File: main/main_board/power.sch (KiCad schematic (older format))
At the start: 18 parts

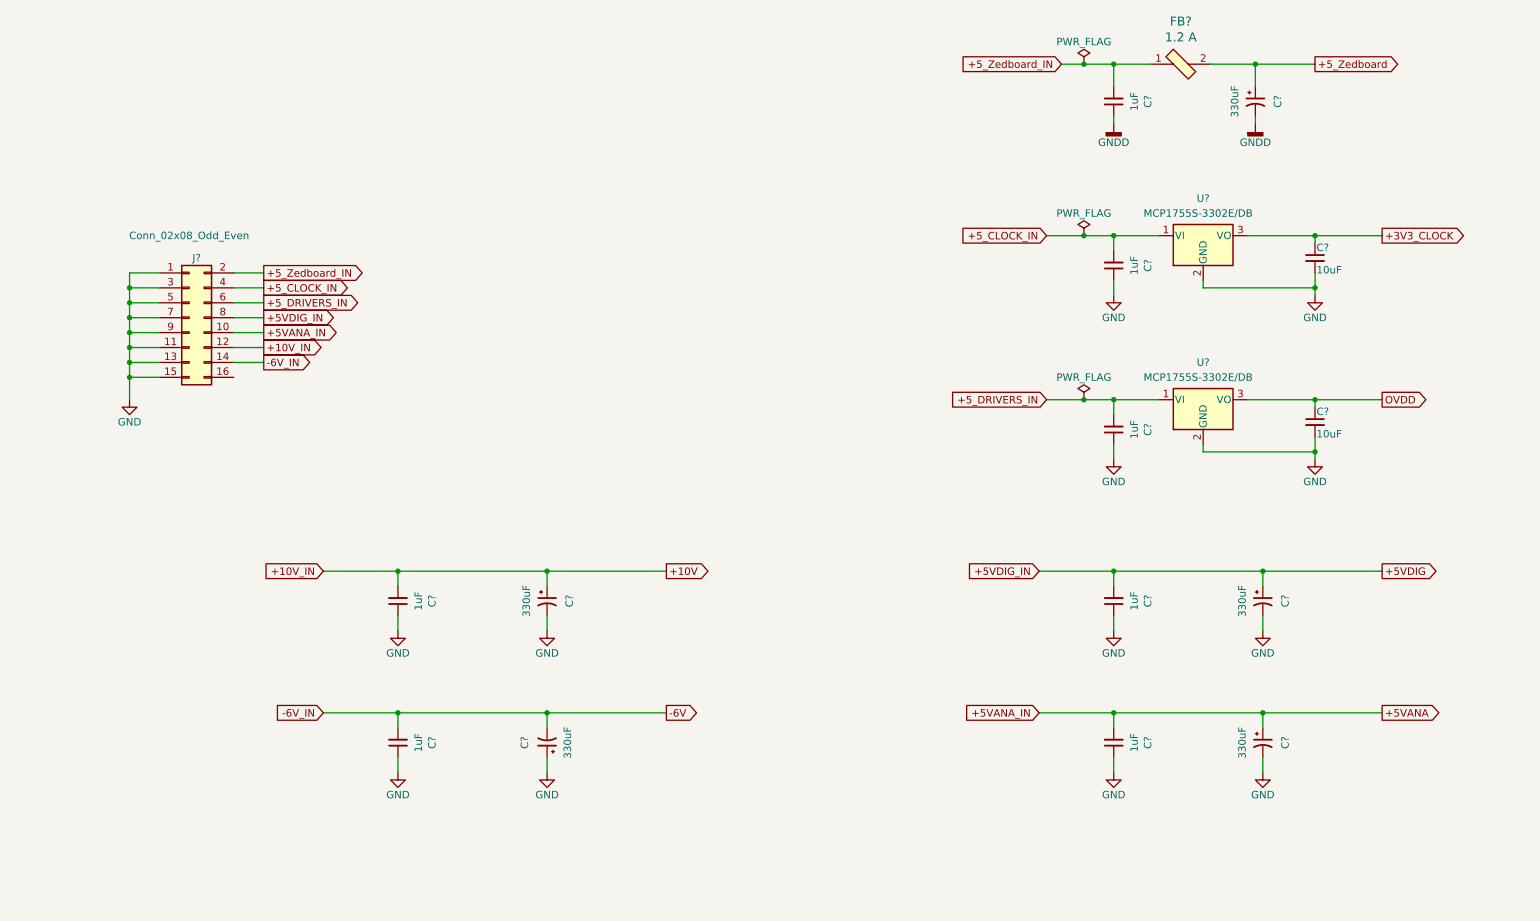
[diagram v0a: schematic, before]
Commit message: Diffs mainly due to first annotation of some new components.  Also changes on power.sch, added TVS and some caps.
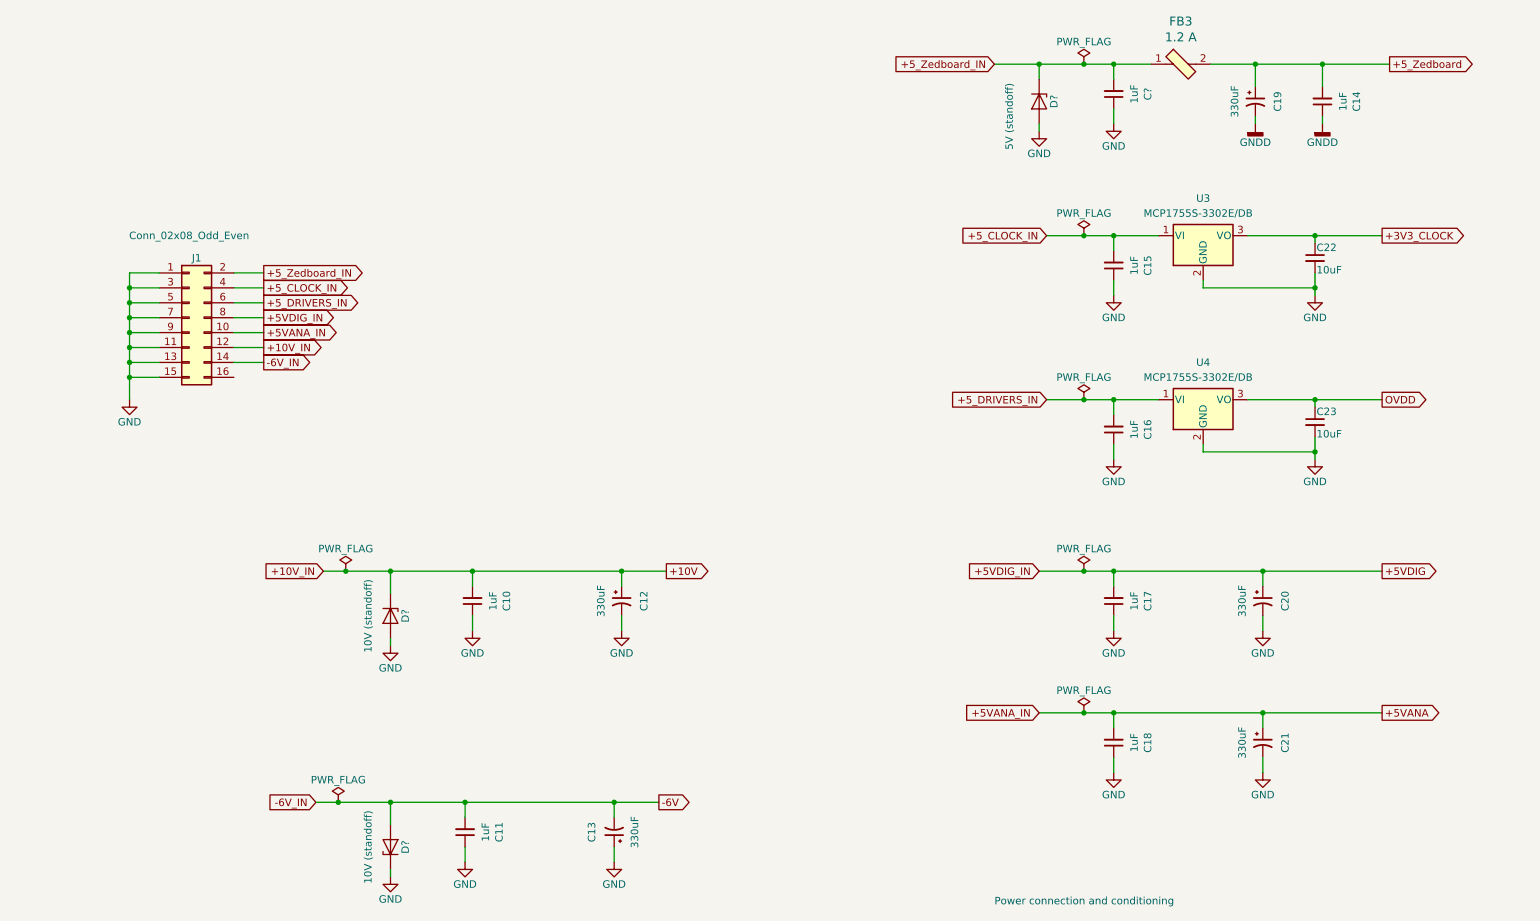
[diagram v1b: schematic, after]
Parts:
- added C?: 1uF, Capacitor_SMD:C_0805_2012Metric, symbol Device:C_Small
- added D?: 5V (standoff), Diode_SMD:D_SMA, symbol Device:D_Zener
- added D? (x2): 10V (standoff), Diode_SMD:D_SMA, symbol Device:D_Zener
- gave numbers to parts that had none: 18
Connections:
- net +10V: now also D?.1 (K)
- net +5_Zedboard: now also C14.2
- net +5_Zedboard_IN: now also C?.2, D?.1 (K); no longer C14.2
- net -6V: now also D?.2 (A)
- net GND: now also C?.1, D?.1 (K), D?.2 (A), D?.2 (A)
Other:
- note added: "Power connection and conditioning"
- moved on the sheet: C10, C11, C12, C13, C14

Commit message: Mostly work on hooking in the Microzed using kipart symbols and a footprint. Also added 2.5V VCCIO regulator.
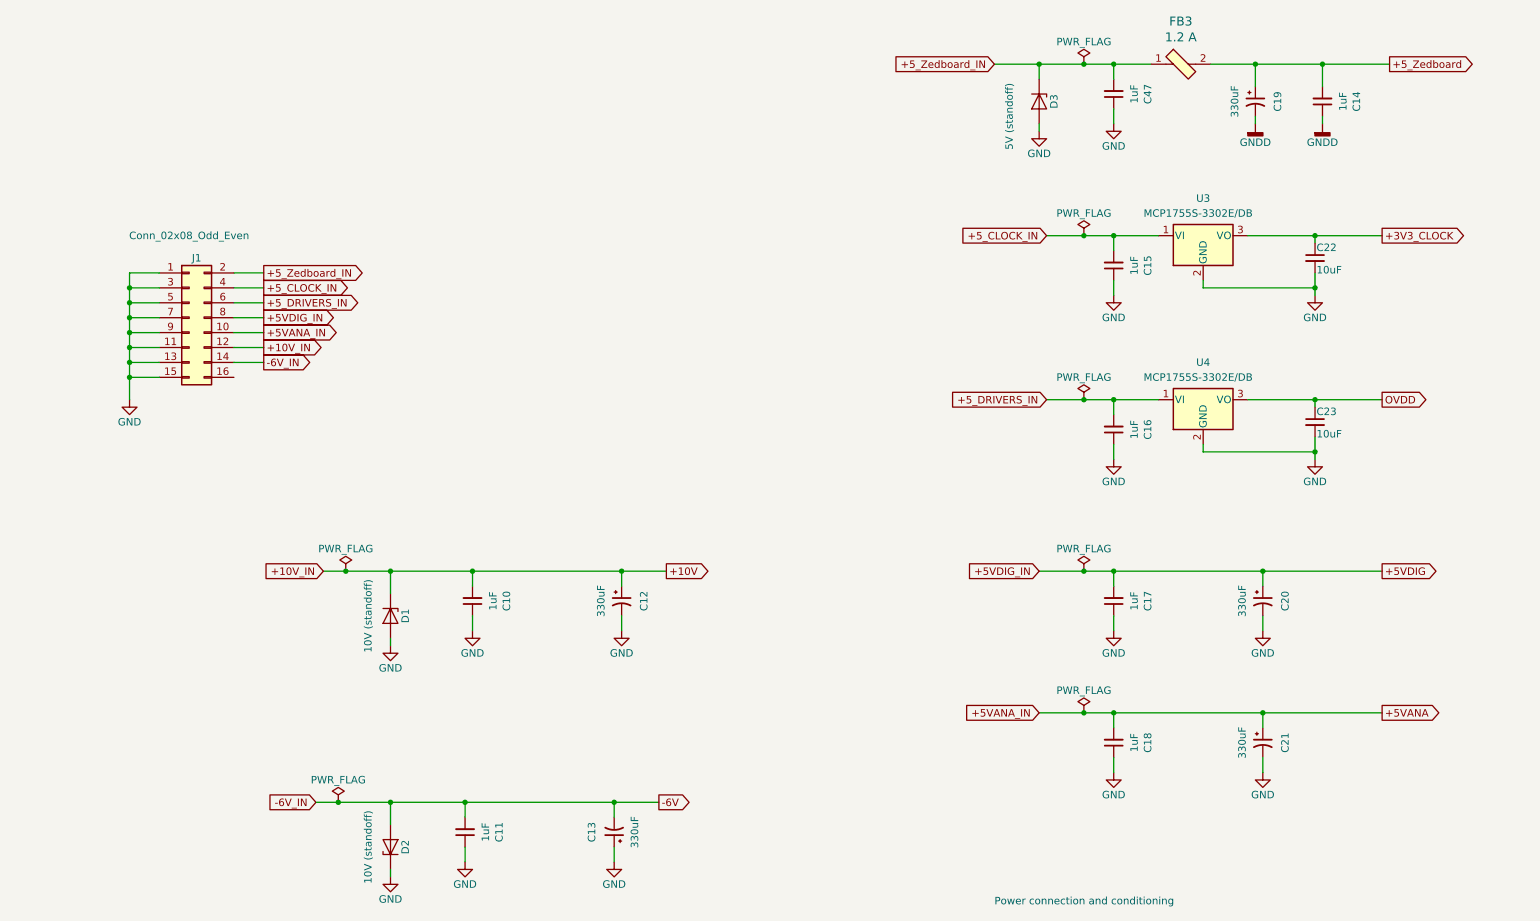
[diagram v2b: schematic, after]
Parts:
- J1: footprint (none) -> Connector_PinHeader_2.54mm:PinHeader_2x08_P2.54mm_Vertical
- gave numbers to parts that had none: 4
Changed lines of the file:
@@
 F 0 "J1" H 1950 3300 50  0000 C CNN
 F 1 "Conn_02x08_Odd_Even" H 1900 3450 50  0000 C CNN
-F 2 "" H 1900 2900 50  0001 C CNN
+F 2 "Connector_PinHeader_2.54mm:PinHeader_2x08_P2.54mm_Vertical" H 1900 2900 50  0001 C CNN
 F 3 "~" H 1900 2900 50  0001 C CNN
 	1    1900 2900
@@
 AR Path="/5E624B3C/5E51E83D/5EE30578" Ref="C?"  Part="1"
 AR Path="/5E525F2C/5EE30578" Ref="C?"  Part="1"
-AR Path="/5E525FC9/5EE30578" Ref="C?"  Part="1"
-F 0 "C?" V 7871 1400 50  0000 C CNN
+AR Path="/5E525FC9/5EE30578" Ref="C47"  Part="1"
+F 0 "C47" V 7871 1400 50  0000 C CNN
 F 1 "1uF" V 7962 1400 50  0000 C CNN
 F 2 "Capacitor_SMD:C_0805_2012Metric" H 8100 1400 50  0001 C CNN
@@
 AR Path="/5E624B3C/5E51E83D/5EE30580" Ref="#PWR?"  Part="1"
 AR Path="/5E525F2C/5EE30580" Ref="#PWR?"  Part="1"
-AR Path="/5E525FC9/5EE30580" Ref="#PWR?"  Part="1"
-F 0 "#PWR?" H 8100 1350 50  0001 C CNN
+AR Path="/5E525FC9/5EE30580" Ref="#PWR051"  Part="1"
+F 0 "#PWR051" H 8100 1350 50  0001 C CNN
 F 1 "GND" H 8100 1450 50  0000 C CNN
 F 2 "" H 8100 1600 50  0001 C CNN
@@
 Power connection and conditioning
 $Comp
-L Device:D_Zener D?
+L Device:D_Zener D3
 U 1 1 5ED00659
 P 7600 1450
-F 0 "D?" H 7600 1550 50  0000 C CNN
+F 0 "D3" H 7600 1550 50  0000 C CNN
 F 1 "5V (standoff)" H 7700 1250 50  0000 C CNN
 F 2 "Diode_SMD:D_SMA" H 7600 1450 50  0001 C CNN
@@
 AR Path="/5E624B3C/5E51E83D/5ED00664" Ref="D?"  Part="1"
 AR Path="/5E62FD57/5E630FEC/5ED00664" Ref="D?"  Part="1"
-AR Path="/5E525FC9/5ED00664" Ref="D?"  Part="1"
-F 0 "D?" H 3250 5000 50  0000 C CNN
+AR Path="/5E525FC9/5ED00664" Ref="D1"  Part="1"
+F 0 "D1" H 3250 5000 50  0000 C CNN
 F 1 "10V (standoff)" H 3250 4750 50  0000 C CNN
 F 2 "Diode_SMD:D_SMA" H 3250 4900 50  0001 C CNN
@@
 AR Path="/5E624B3C/5E51E83D/5ED1A5E4" Ref="#PWR?"  Part="1"
 AR Path="/5E525F2C/5ED1A5E4" Ref="#PWR?"  Part="1"
-AR Path="/5E525FC9/5ED1A5E4" Ref="#PWR?"  Part="1"
-F 0 "#PWR?" H 3250 4850 50  0001 C CNN
+AR Path="/5E525FC9/5ED1A5E4" Ref="#PWR045"  Part="1"
+F 0 "#PWR045" H 3250 4850 50  0001 C CNN
 F 1 "GND" H 3250 4950 50  0000 C CNN
 F 2 "" H 3250 5100 50  0001 C CNN
@@
 AR Path="/5E624B3C/5E51E83D/5ED1DE18" Ref="D?"  Part="1"
 AR Path="/5E62FD57/5E630FEC/5ED1DE18" Ref="D?"  Part="1"
-AR Path="/5E525FC9/5ED1DE18" Ref="D?"  Part="1"
-F 0 "D?" H 3250 6350 50  0000 C CNN
+AR Path="/5E525FC9/5ED1DE18" Ref="D2"  Part="1"
+F 0 "D2" H 3250 6350 50  0000 C CNN
 F 1 "10V (standoff)" H 3250 6600 50  0000 C CNN
 F 2 "Diode_SMD:D_SMA" H 3250 6450 50  0001 C CNN
@@
 AR Path="/5E624B3C/5E51E83D/5ED1DE1F" Ref="#PWR?"  Part="1"
 AR Path="/5E525F2C/5ED1DE1F" Ref="#PWR?"  Part="1"
-AR Path="/5E525FC9/5ED1DE1F" Ref="#PWR?"  Part="1"
-F 0 "#PWR?" H 3250 6400 50  0001 C CNN
+AR Path="/5E525FC9/5ED1DE1F" Ref="#PWR047"  Part="1"
+F 0 "#PWR047" H 3250 6400 50  0001 C CNN
 F 1 "GND" H 3250 6500 50  0000 C CNN
 F 2 "" H 3250 6650 50  0001 C CNN
@@
 AR Path="/5E624B3C/5E51E83D/5ED238AD" Ref="#FLG?"  Part="1"
 AR Path="/5E525F2C/5ED238AD" Ref="#FLG?"  Part="1"
-AR Path="/5E525FC9/5ED238AD" Ref="#FLG?"  Part="1"
-F 0 "#FLG?" H 2950 4675 50  0001 C CNN
+AR Path="/5E525FC9/5ED238AD" Ref="#FLG06"  Part="1"
+F 0 "#FLG06" H 2950 4675 50  0001 C CNN
 F 1 "PWR_FLAG" H 2950 4750 50  0000 C CNN
 F 2 "" H 2950 4600 50  0001 C CNN
@@
 AR Path="/5E624B3C/5E51E83D/5ED24044" Ref="#FLG?"  Part="1"
 AR Path="/5E525F2C/5ED24044" Ref="#FLG?"  Part="1"
-AR Path="/5E525FC9/5ED24044" Ref="#FLG?"  Part="1"
-F 0 "#FLG?" H 2900 6225 50  0001 C CNN
+AR Path="/5E525FC9/5ED24044" Ref="#FLG05"  Part="1"
+F 0 "#FLG05" H 2900 6225 50  0001 C CNN
 F 1 "PWR_FLAG" H 2900 6300 50  0000 C CNN
 F 2 "" H 2900 6150 50  0001 C CNN
@@
 AR Path="/5E624B3C/5E51E83D/5ED243FE" Ref="#FLG?"  Part="1"
 AR Path="/5E525F2C/5ED243FE" Ref="#FLG?"  Part="1"
-AR Path="/5E525FC9/5ED243FE" Ref="#FLG?"  Part="1"
-F 0 "#FLG?" H 7900 5625 50  0001 C CNN
+AR Path="/5E525FC9/5ED243FE" Ref="#FLG08"  Part="1"
+F 0 "#FLG08" H 7900 5625 50  0001 C CNN
 F 1 "PWR_FLAG" H 7900 5700 50  0000 C CNN
 F 2 "" H 7900 5550 50  0001 C CNN
@@
 AR Path="/5E624B3C/5E51E83D/5ED24891" Ref="#FLG?"  Part="1"
 AR Path="/5E525F2C/5ED24891" Ref="#FLG?"  Part="1"
-AR Path="/5E525FC9/5ED24891" Ref="#FLG?"  Part="1"
-F 0 "#FLG?" H 7900 4675 50  0001 C CNN
+AR Path="/5E525FC9/5ED24891" Ref="#FLG07"  Part="1"
+F 0 "#FLG07" H 7900 4675 50  0001 C CNN
 F 1 "PWR_FLAG" H 7900 4750 50  0000 C CNN
 F 2 "" H 7900 4600 50  0001 C CNN
@@
 AR Path="/5E624B3C/5E51E83D/5ED2A5F8" Ref="#PWR?"  Part="1"
 AR Path="/5E525F2C/5ED2A5F8" Ref="#PWR?"  Part="1"
-AR Path="/5E525FC9/5ED2A5F8" Ref="#PWR?"  Part="1"
-F 0 "#PWR?" H 7600 1400 50  0001 C CNN
+AR Path="/5E525FC9/5ED2A5F8" Ref="#PWR048"  Part="1"
+F 0 "#PWR048" H 7600 1400 50  0001 C CNN
 F 1 "GND" H 7600 1500 50  0000 C CNN
 F 2 "" H 7600 1650 50  0001 C CNN

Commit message: Schematic is mostly complete (except for BIST DACs), and passes ERC.  Rough placement of components on PCB.
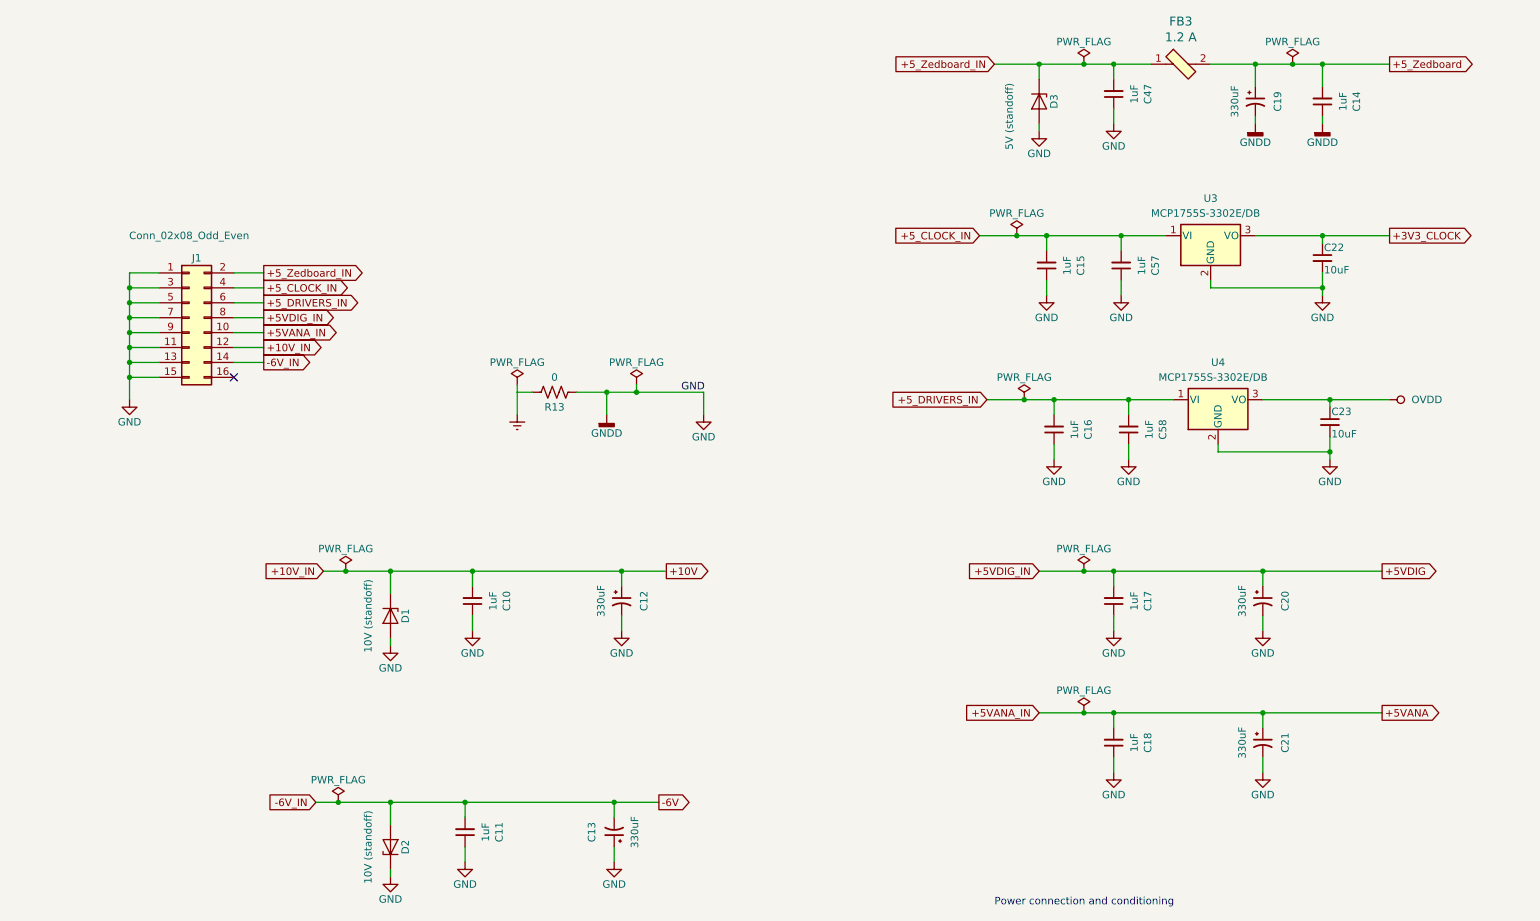
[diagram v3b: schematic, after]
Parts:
- added C57, C58: 1uF, Capacitor_SMD:C_0805_2012Metric, symbol Device:C_Small
- added R13: 0, Resistor_SMD:R_0603_1608Metric, symbol Device:R_US
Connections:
- net GNDD is gone; now on net GND: C14.1, C19.2
- net +5_CLOCK_IN: now also C57.2
- net +5_DRIVERS_IN: now also C58.2
- net GND: now also C57.1, C58.1, R13.1
- new net Earth: R13.2
- no-connect marks 0 -> 1
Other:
- moved on the sheet: C15, C16, C22, C23, U3, U4

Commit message: Mechanical feature layout on main board (edge connector and mount hole locations).  Added some dimension callouts to the input board. Tweaked grounding on main board schematic.  Chassis ground is not connected to main board ground except via an optional capacitor.  Chassis ground comes in on the power connector. Added BIST DAC, including additions to power.sch and input_slots.sch.
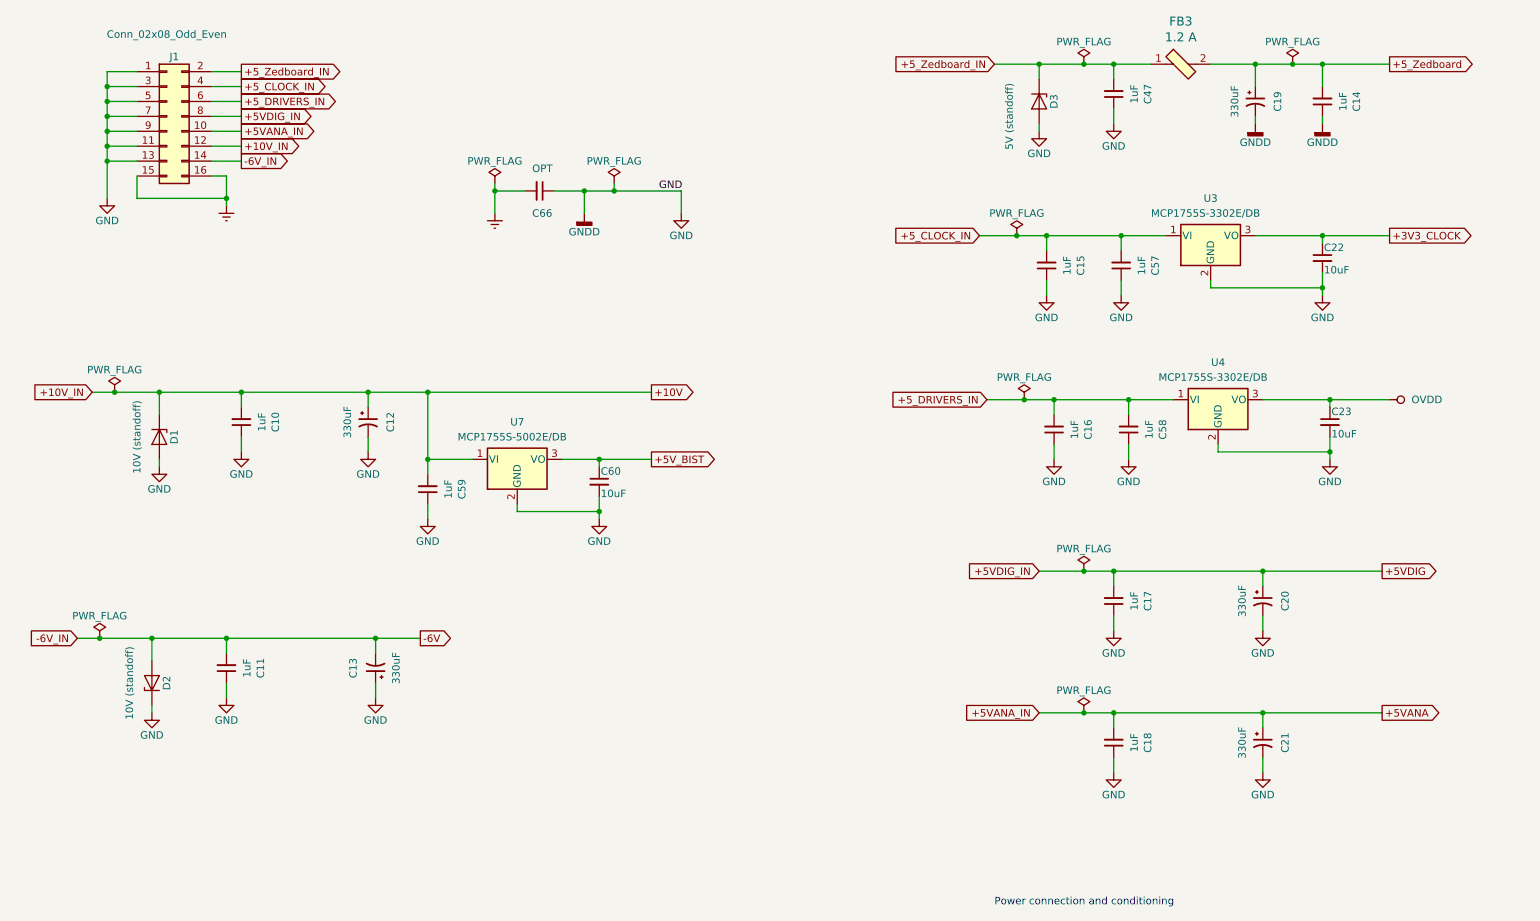
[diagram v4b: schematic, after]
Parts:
- removed R13: 0, Resistor_SMD:R_0603_1608Metric, symbol Device:R_US
- added C59: 1uF, Capacitor_SMD:C_0805_2012Metric, symbol Device:C_Small
- added C60: 10uF, Capacitor_SMD:C_0603_1608Metric, symbol Device:C_Small
- added C66: OPT, Capacitor_SMD:C_0603_1608Metric, symbol Device:C_Small
- added U7: MCP1755S-5002E/DB, Package_TO_SOT_SMD:SOT-223-3_TabPin2, symbol Regulator_Linear:MCP1703A-1202_SOT223
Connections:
- net +10V: now also C59.2, U7.1 (VI)
- net Earth: now also J1.15 (Pin_15), J1.16 (Pin_16), C66.2
- net GND: now also C59.1, C60.2, C66.1, U7.2 (GND); no longer J1.15 (Pin_15)
- new net +5V_BIST: C60.1, U7.3 (VO)
- no-connect marks 1 -> 0
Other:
- moved on the sheet: C10, C11, C12, C13, D1, D2, J1
